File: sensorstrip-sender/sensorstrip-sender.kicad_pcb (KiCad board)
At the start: 2 copper layers, 56 x 12 mm, 13 parts, among them J1 USB_C_Receptacle_PowerOnly, J2 Conn_01x02_MountingPin, SW1 SW_DPDT_x2

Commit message: of course i ran drc before pushing what do you take me for
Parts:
- moved R1 0.31 mm to (137.8, 52.9)
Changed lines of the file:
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@@
   (net 8 "/Power_postFuse")
   (footprint "Resistor_SMD:R_0805_2012Metric_Pad1.20x1.40mm_HandSolder" (layer "F.Cu")
-    (at 137.6 53.2)
+    (at 137.75 52.925)
     (descr "Resistor SMD 0805 (2012 Metric), square (rectangular) end terminal, IPC_7351 nominal with elongated pad for handsoldering. (Body size source: IPC-SM-782 page 72, https://www.pcb-3d.com/wordpress/wp-content/uploads/ipc-sm-782a_amendment_1_and_2.pdf), generated with kicad-footprint-generator")
     (tags "resistor handsolder")
@@
   (segment (start 128.465 53.2) (end 129.235 53.97) (width 0.6) (layer "F.Cu") (net 4))
   (segment (start 135.27 53.99) (end 134.48 53.2) (width 0.6) (layer "F.Cu") (net 4))
+  (segment (start 139.375 52.3) (end 138.75 52.925) (width 0.6) (layer "F.Cu") (net 5))
   (segment (start 115.225 55.6) (end 115.225 53.225) (width 0.6) (layer "F.Cu") (net 5))
   (segment (start 102.53 59.35) (end 102.53 53.85) (width 0.6) (layer "F.Cu") (net 5))
-  (segment (start 140 52.3) (end 139.5 52.3) (width 0.6) (layer "F.Cu") (net 5))
-  (segment (start 139.5 52.3) (end 138.6 53.2) (width 0.6) (layer "F.Cu") (net 5))
   (segment (start 115.225 53.225) (end 114.8 52.8) (width 0.6) (layer "F.Cu") (net 5))
+  (segment (start 140 52.3) (end 139.375 52.3) (width 0.6) (layer "F.Cu") (net 5))
   (segment (start 102.7 53.25) (end 102.7 51.4) (width 0.6) (layer "F.Cu") (net 5))
   (via (at 102.7 51.4) (size 0.8) (drill 0.4) (layers "F.Cu" "B.Cu") (net 5))

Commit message: fix humongous oversight
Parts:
- added ?: , , F.Cu at (114.0, 52.5)
- added ?: , , F.Cu at (115.5, 52.5)
- moved R2 12.3 mm to (138.5, 54.1), turned to 0 degrees
- moved D1 12.0 mm to (122.0, 59.0)
- moved D3 12.0 mm to (134.0, 59.0)
- moved R3 8.27 mm to (138.5, 55.9)
- moved F1 5.80 mm to (128.0, 51.0)
- moved ? 2.01 mm to (151.7, 59.4)
- moved R1 1.02 mm to (138.3, 52.1)
- moved D2 1.00 mm to (128.0, 59.0)
- moved JP1 0.75 mm to (103.8, 55.5)
- moved SW1 0.75 mm to (105.0, 55.5)
- renumbered D3 to D1, D1 to D3
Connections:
- D1 pad 2: /LEDs -> /D1+
- D2 pad 1: GND -> /D1+
- D2 pad 2: /LEDs -> /D2+
- D3 pad 1: GND -> /D2+
- D3 pad 2: /LEDs -> /D3+
- R1 pad 1: /LEDs -> /D3+
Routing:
- net /LEDs: track 28.9 -> 0.00 mm
- net /CC1: track 2.99 -> 11.4 mm, vias 0 -> 2
- net /D3+: track 0.00 -> 7.76 mm
- net /CC2: track 3.35 -> 9.89 mm, vias 0 -> 2
- net /VBUS: track 39.9 -> 34.1 mm
- net /Power_postFuse: track 23.7 -> 27.9 mm
- net /D1+: track 0.00 -> 3.46 mm
- net /D2+: track 0.00 -> 3.46 mm
- net GND: track 0.00 -> 3.22 mm, vias 3 -> 2
- net Power_postSwitch: track 11.8 -> 12.1 mm, vias 3 -> 2
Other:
- board size 56 x 12 mm -> 56 x 13 mm
- board text added: "+"
- board text added: "-"

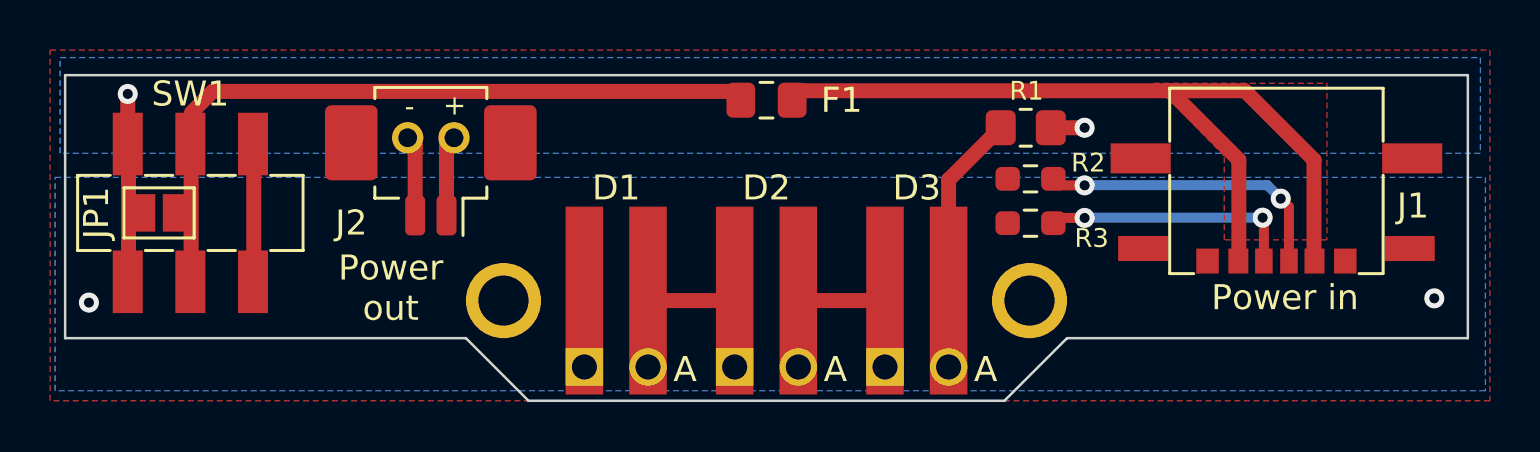
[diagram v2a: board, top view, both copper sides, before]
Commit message: Cleanup in preparation for push
Update project files to KiCad 7 format
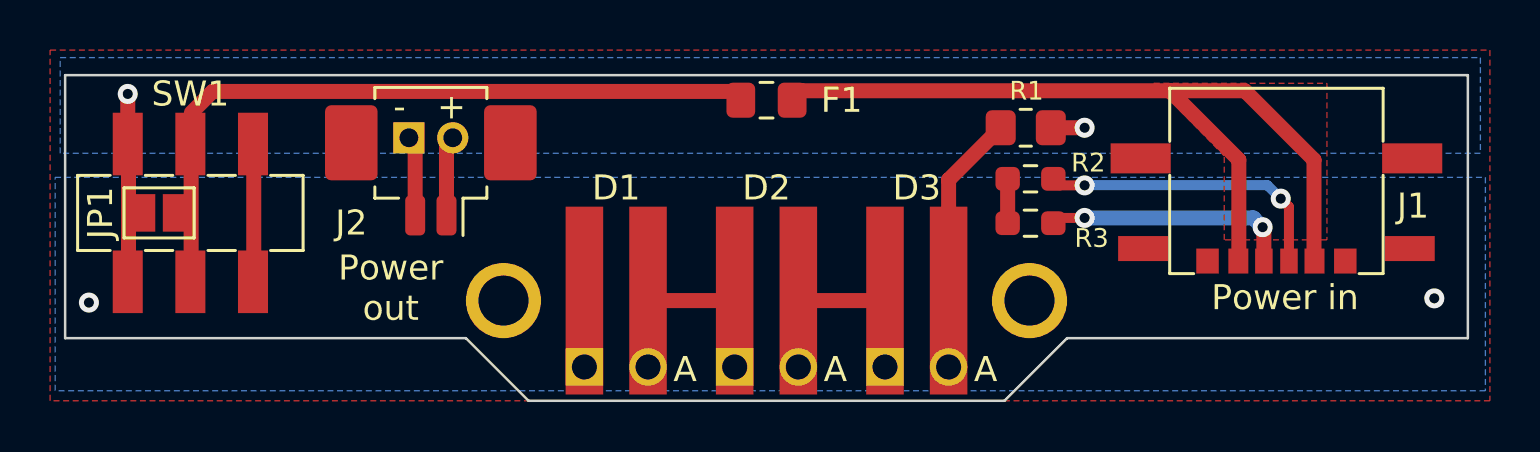
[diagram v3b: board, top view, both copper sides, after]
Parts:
- removed the ? at (107.3, 59.8)
- removed the ? at (151.7, 59.4)
- removed the ? at (114.0, 52.5)
- removed the ? at (115.5, 52.5)
- added ?: MountingHole-2mm-PTH, sensorstrip:MountingHole-2mm-PTH, F.Cu at (117.5, 59.0)
- added ?: MountingHole-2mm-PTH, sensorstrip:MountingHole-2mm-PTH, F.Cu at (138.5, 59.0)
- added REF**: Power-P1.75mm, sensorstrip:Power-P1.75mm, F.Cu at (114.6, 52.5)
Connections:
- SW1 pad 3: unconnected-(SW1-Pad3) -> Net-(SW1A-C)
- SW1 pad 6: unconnected-(SW1-Pad3) -> Net-(SW1A-C)
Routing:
- net unconnected-(SW1-Pad3): track 5.50 -> 0.00 mm
- net Net-(SW1A-C): track 0.00 -> 5.50 mm
- net GND: track 3.22 -> 4.57 mm
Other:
- board text removed: "+"
- board text removed: "-"
